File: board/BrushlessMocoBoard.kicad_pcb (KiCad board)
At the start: 4 copper layers, 115 parts, among them SW1 SW_Push, SW2 SW_Push, U1 STSPIN32G4TR, U2 SN65HVD232

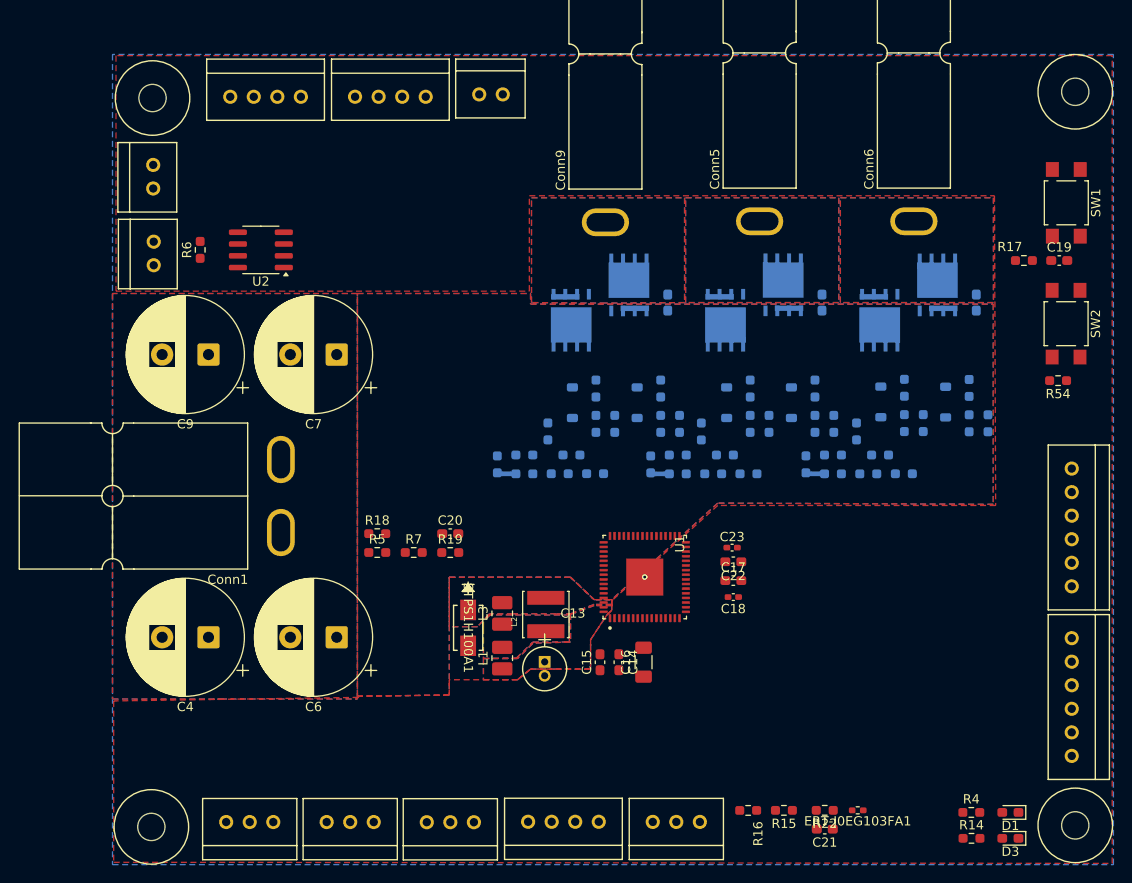
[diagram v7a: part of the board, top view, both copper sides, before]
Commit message: First draft of wiring for the layout finished.
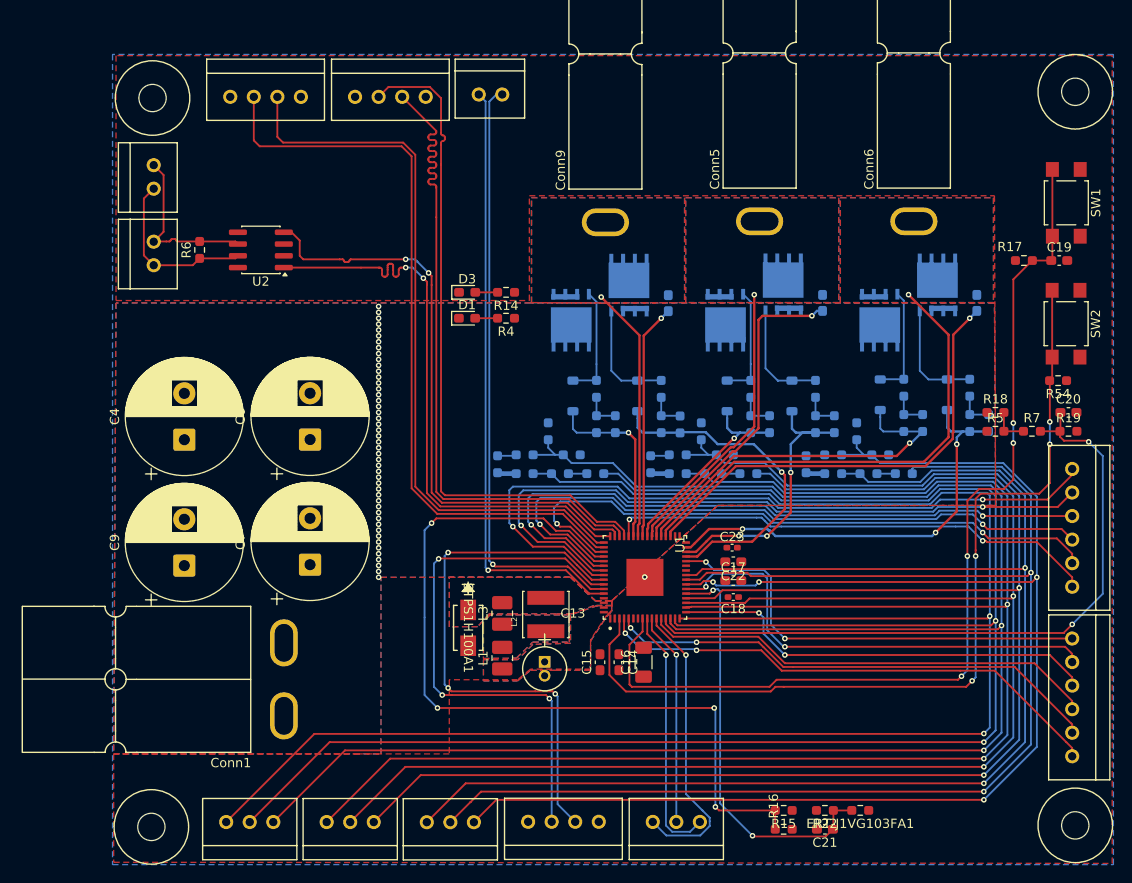
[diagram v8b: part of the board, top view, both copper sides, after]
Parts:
- ERT-J1VG103FA1: renamed from ERT-J0EG103FA1; footprint Resistor_SMD:R_0402_1005Metric_Pad0.72x0.64mm_HandSolder -> Resistor_SMD:R_0603_1608Metric_Pad0.98x0.95mm_HandSolder
- moved D3 83.1 mm to (68.0, 65.8), turned to 0 degrees
- moved D1 79.2 mm to (68.0, 68.6), turned to 0 degrees
- moved R14 77.4 mm to (72.2, 65.8), turned to 180 degrees
- moved R4 73.2 mm to (72.2, 68.6), turned to 180 degrees
- moved R19 67.9 mm to (132.8, 80.8)
- moved R7 67.9 mm to (128.9, 80.8)
- moved C20 67.9 mm to (132.8, 78.7)
- moved R18 67.9 mm to (124.9, 78.7)
- moved R5 67.9 mm to (124.9, 80.8)
- moved C9 22.9 mm to (37.5, 95.3), turned to 90 degrees
- moved C7 22.8 mm to (51.0, 95.2), turned to 90 degrees
- moved C6 21.5 mm to (51.0, 81.7), turned to 90 degrees
- moved C4 21.5 mm to (37.5, 81.7), turned to 90 degrees
- moved Conn1 19.8 mm to (48.3, 103.3)
- moved R16 4.34 mm to (102.1, 123.7), turned to 0 degrees
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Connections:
- Conn12 pad 1: /Interfaces/I/O_PA4 -> /Interfaces/I/O_PB5
- Conn12 pad 2: /Interfaces/I/O_PA8 -> /Interfaces/I/O_PB4
- Conn12 pad 3: /Interfaces/I/O_PA15 -> /Interfaces/I/O_PB3
- Conn12 pad 4: /Interfaces/I/O_PB3 -> /Interfaces/I/O_PD2
- Conn12 pad 5: /Interfaces/I/O_PB4 -> /Interfaces/I/O_PA15
- Conn12 pad 6: /Interfaces/I/O_PB5 -> /Interfaces/I/O_PA8
- Conn13 pad 1: /Interfaces/I/O_PC3 -> /Interfaces/I/O_PB10
- Conn13 pad 3: /Interfaces/I/O_PC14 -> /Interfaces/I/O_PA4
- Conn13 pad 4: /Interfaces/I/O_PC15 -> /Interfaces/I/O_PC3
- Conn13 pad 5: /Interfaces/I/O_PD2 -> /Interfaces/I/O_PC15
- Conn13 pad 6: /Interfaces/I/O_PB10 -> /Interfaces/I/O_PC14
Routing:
- net /Half-Bridges & Current Sensing/OPP_U: track 0.00 -> 200.1 mm, vias 0 -> 2
- net /Half-Bridges & Current Sensing/OPN_U: track 0.00 -> 196.5 mm, vias 0 -> 2
- net /Half-Bridges & Current Sensing/OPO_U: track 0.00 -> 189.5 mm, vias 0 -> 2
- net /Half-Bridges & Current Sensing/OPP_V: track 0.00 -> 176.8 mm, vias 0 -> 2
- net /Half-Bridges & Current Sensing/OPN_V: track 0.00 -> 174.8 mm, vias 0 -> 2
- net /Half-Bridges & Current Sensing/OPO_V: track 0.00 -> 166.7 mm, vias 0 -> 2
- net /Half-Bridges & Current Sensing/OPP_W: track 0.00 -> 154.5 mm, vias 0 -> 4
- net /Half-Bridges & Current Sensing/OPN_W: track 0.00 -> 153.3 mm, vias 0 -> 2
- net /Half-Bridges & Current Sensing/OPO_W: track 0.00 -> 145.4 mm, vias 0 -> 2
- net Net-(U1-PG10): track 0.00 -> 105.6 mm, vias 0 -> 4
- net Net-(U1-PC13): track 0.00 -> 96.3 mm, vias 0 -> 4
- net Net-(U1-SCREF): track 0.00 -> 90.7 mm, vias 0 -> 4
- net /Interfaces/SWCLK: track 0.00 -> 81.6 mm
- net /Interfaces/I/O_PB5: track 0.00 -> 80.0 mm, vias 0 -> 2
- net /Interfaces/SWDIO: track 0.00 -> 78.6 mm
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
